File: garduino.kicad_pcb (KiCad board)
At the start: 2 copper layers, 107 parts, among them M1 PT2272, M2 PT2272, P1 GS009S, P10 GS009S, P11 3pin 3.5mm jack, P12 3pin 3.5mm jack, P13 3pin 3.5mm jack, P14 3pin 3.5mm jack, P2 3way KK, P3 GS009S, P4 GS009S, P5 GS009S, P6 GS009S, P7 GS009S, P8 GS009S, P9 GS009S, Q1 CJ2302, Q10 FDN340P, Q2 PSMN6R0, Q3 PSMN6R0, Q4 PSMN6R0, Q5 PSMN6R0, Q6 PSMN6R0, Q7 PSMN6R0, Q8 PSMN6R0, Q9 PSMN6R0, U1 DS1339, U2 24AA16T, U3 74AHCT244, U4 MCP9700, U5 74AHC1G02, U6 74HCT165, U7 74AHCT1G125, Y1 32.768kHz

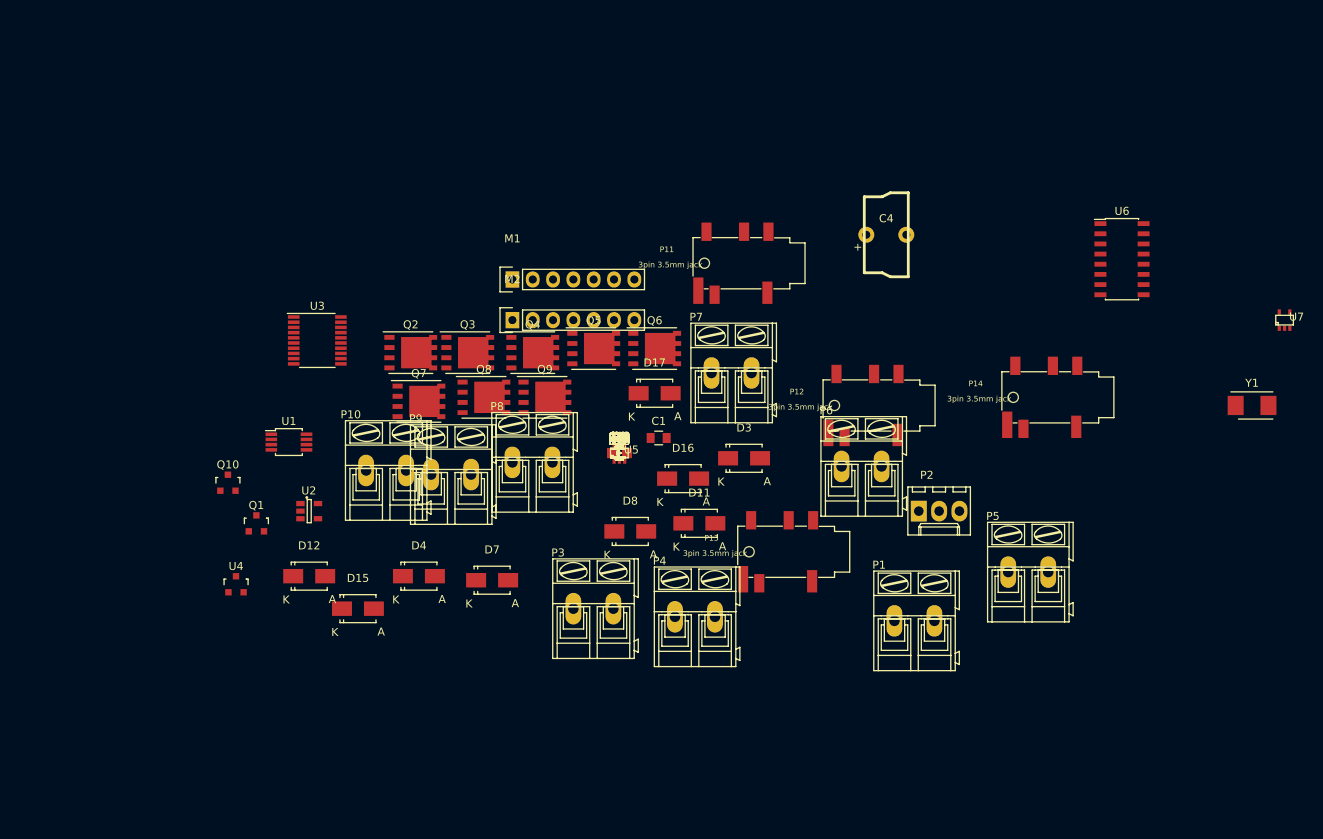
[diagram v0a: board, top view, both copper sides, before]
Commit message: Laid out parts and routed some of the signals
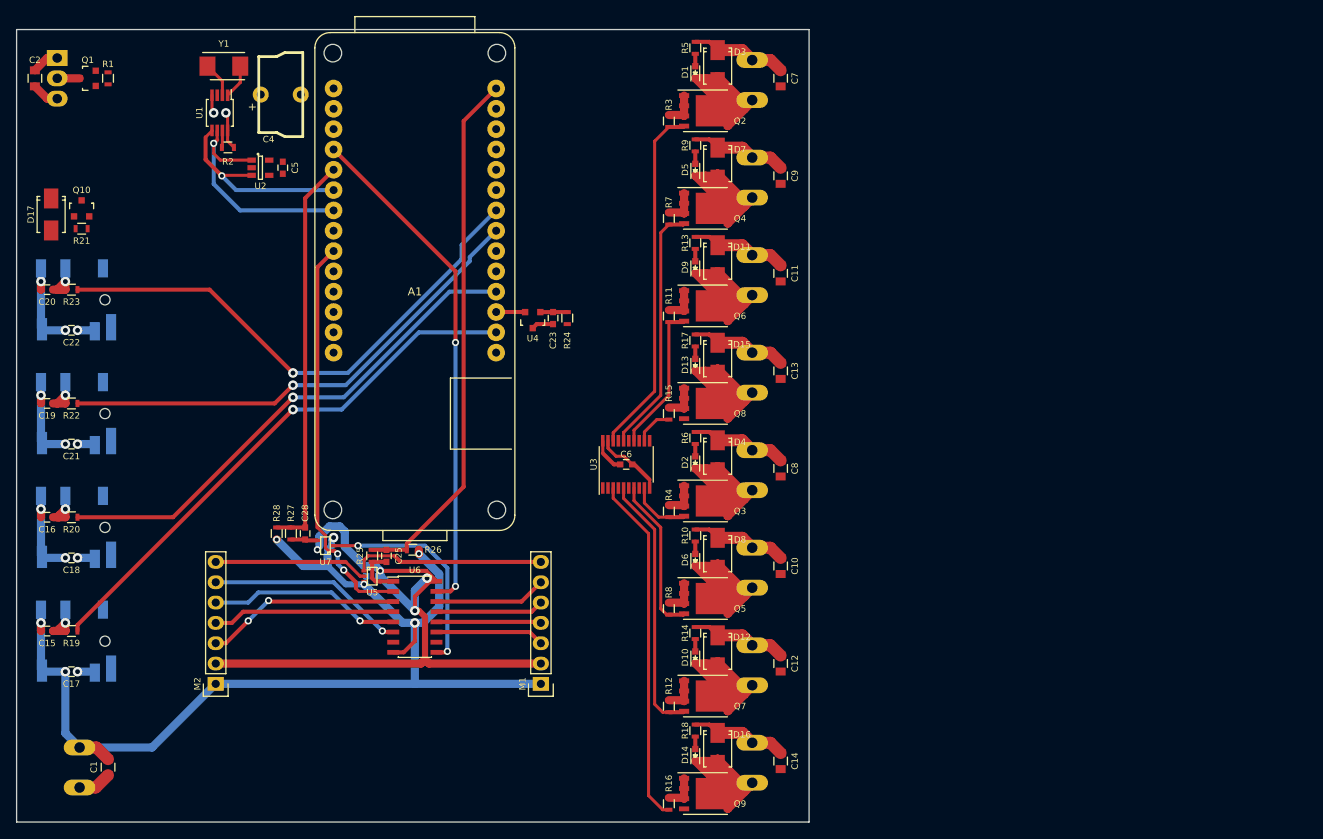
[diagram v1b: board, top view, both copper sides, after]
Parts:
- added A1: ARDUINO_MKR1000, jakub:ARDUINO_MKR1000, F.Cu at (122.9, 83.6)
- C24, C26, C27, C3, P1, P10, P2, P3, P4, P5, P6, P7, P8, P9: moved to B.Cu
- P11: renamed from P14; moved to B.Cu
- P12: renamed from P13; moved to B.Cu
- P13: renamed from P12; moved to B.Cu
- P14: renamed from P11; moved to B.Cu
- moved Y1 135.3 mm to (99.1, 56.6)
- moved P11 127.2 mm to (79.2, 128.5), turned to 180 degrees
- moved U7 123.2 mm to (111.8, 116.6), turned to 90 degrees
- moved P2 121.7 mm to (78.2, 55.6), turned to 270 degrees
- moved P1 104.0 mm to (81.0, 146.8), turned to 90 degrees
- moved P13 101.1 mm to (79.2, 100.1), turned to 180 degrees
- moved U6 99.1 mm to (122.9, 125.5)
- moved P12 90.5 mm to (79.2, 114.3), turned to 180 degrees
- moved C2 86.8 mm to (75.4, 58.2), turned to 270 degrees
- moved P14 85.0 mm to (79.2, 85.9), turned to 180 degrees
- moved C1 80.2 mm to (84.6, 144.3), turned to 90 degrees
- moved R1 79.2 mm to (84.6, 58.2), turned to 90 degrees
- moved D17 78.7 mm to (77.5, 75.2), turned to 270 degrees
- moved C4 77.7 mm to (106.2, 60.2)
- moved C15 74.9 mm to (77.0, 127.3), turned to 180 degrees
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- renumbered C20 to C15, C19 to C16, C22 to C17, C21 to C18, C16 to C19, C15 to C20, C18 to C21, C17 to C22, R23 to R19, R22 to R20, R20 to R22, R19 to R23
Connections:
- D17 pad 1: (no net) -> /Sensors/~SENS
- P11 pad LS: (no net) -> Net-(P11-PadLS)
- P11 pad RS: (no net) -> Net-(P11-PadRS)
- P12 pad LS: (no net) -> Net-(P12-PadLS)
- P12 pad RS: (no net) -> Net-(P12-PadRS)
- P13 pad LS: (no net) -> Net-(P13-PadLS)
- P13 pad RS: (no net) -> Net-(P13-PadRS)
- P14 pad LS: (no net) -> Net-(P14-PadLS)
- P14 pad RS: (no net) -> Net-(P14-PadRS)
- Q3 pad 4: /PowerDrivers/OUT4 -> /PowerDrivers/OUT1
- Q4 pad 4: /PowerDrivers/OUT1 -> /PowerDrivers/OUT2
- Q5 pad 4: /PowerDrivers/OUT5 -> /PowerDrivers/OUT3
- Q6 pad 4: /PowerDrivers/OUT2 -> /PowerDrivers/OUT4
- Q7 pad 4: /PowerDrivers/OUT6 -> /PowerDrivers/OUT5
- Q8 pad 4: /PowerDrivers/OUT3 -> /PowerDrivers/OUT6
- R11 pad 1: /PowerDrivers/OUT2 -> /PowerDrivers/OUT4
- R12 pad 1: /PowerDrivers/OUT6 -> /PowerDrivers/OUT5
- R15 pad 1: /PowerDrivers/OUT3 -> /PowerDrivers/OUT6
- R19 pad 2: (no net) -> /Sensors/SENS0
- R20 pad 2: (no net) -> /Sensors/SENS1
- R22 pad 2: (no net) -> /Sensors/SENS2
- R23 pad 2: (no net) -> /Sensors/SENS3
- R4 pad 1: /PowerDrivers/OUT4 -> /PowerDrivers/OUT1
- R7 pad 1: /PowerDrivers/OUT1 -> /PowerDrivers/OUT2
- R8 pad 1: /PowerDrivers/OUT5 -> /PowerDrivers/OUT3
- U3 pad 11: (no net) -> /PowerDrivers/D4
- U3 pad 13: (no net) -> /PowerDrivers/D5
- U3 pad 15: (no net) -> /PowerDrivers/D6
- U3 pad 17: (no net) -> /PowerDrivers/D7
- U3 pad 2: (no net) -> /PowerDrivers/D0
- U3 pad 4: (no net) -> /PowerDrivers/D1
- U3 pad 6: (no net) -> /PowerDrivers/D2
- U3 pad 8: (no net) -> /PowerDrivers/D3
- U4 pad 2: (no net) -> /Sensors/TEMP
- U6 pad 10: (no net) -> Net-(U6-Pad10)
- U6 pad 15: (no net) -> /RFmodules/SCK
- U6 pad 7: (no net) -> Net-(U6-Pad7)
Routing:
- net GND: track 0.00 -> 227.8 mm, vias 0 -> 14
- net +12V: track 0.00 -> 101.3 mm
- net VCC: track 0.00 -> 94.8 mm, vias 0 -> 4
- net /Sensors/SENS0: track 0.00 -> 68.2 mm, vias 0 -> 1
- net /RFmodules/RF_DATA_3V3: track 0.00 -> 66.6 mm
- net /Sensors/SENS3: track 0.00 -> 66.1 mm, vias 0 -> 1
- net /Sensors/SENS1: track 0.00 -> 64.0 mm, vias 0 -> 1
- net /RFmodules/SCK: track 0.00 -> 63.6 mm, vias 0 -> 2
- net /Sensors/SENS2: track 0.00 -> 61.6 mm, vias 0 -> 1
- net /RFmodules/~CS_RF: track 0.00 -> 50.3 mm, vias 0 -> 2
- net /RFmodules/MISO: track 0.00 -> 49.7 mm
- net /PowerDrivers/OUT5: track 0.00 -> 47.9 mm
- net /PowerDrivers/OUT0: track 0.00 -> 44.1 mm
- net /PowerDrivers/OUT7: track 0.00 -> 43.6 mm
- net Net-(D2-Pad1): track 0.00 -> 38.5 mm
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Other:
- board outline added: 99.1 x 99.1 mm
